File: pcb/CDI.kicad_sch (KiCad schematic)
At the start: 20 parts, among them Q1 MMBT2222A

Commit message: small fix
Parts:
- C9: footprint Capacitor_THT:CP_Axial_L18.0mm_D8.0mm_P25.00mm_Horizontal -> Capacitor_THT:C_Axial_L12.0mm_D7.5mm_P20.00mm_Horizontal
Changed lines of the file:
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@@
 			)
 		)
-		(property "Footprint" "Capacitor_THT:CP_Axial_L18.0mm_D8.0mm_P25.00mm_Horizontal"
+		(property "Footprint" "Capacitor_THT:C_Axial_L12.0mm_D7.5mm_P20.00mm_Horizontal"
 			(at 224.79 51.1048 0)
 			(effects

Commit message: video call revision
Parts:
- removed C10: 100n, Capacitor_SMD:C_0201_0603Metric, symbol Device:C
- removed JP6: SolderJumper_2_Open, Jumper:SolderJumper-2_P1.3mm_Open_RoundedPad1.0x1.5mm, symbol Jumper:SolderJumper_2_Open
- removed R14: 130R, Resistor_THT:R_Axial_DIN0204_L3.6mm_D1.6mm_P1.90mm_Vertical, symbol Device:R
- removed R16: 100R, Resistor_THT:R_Axial_DIN0204_L3.6mm_D1.6mm_P1.90mm_Vertical, symbol Device:R
- removed R17: 47k, Resistor_SMD:R_0201_0603Metric, symbol Device:R
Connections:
- net GND is gone; now on an unnamed net: Q1.2 (E)
- net +5V: now also Q1.3 (C)
- net at R13.1: no longer Q1.3 (C)
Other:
- note removed: "GATE SNUBBER"
- moved on the sheet: Q1, R15, TP9

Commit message: added footprints
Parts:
- D2: footprint TN1215800GTR -> SamacSys_Parts:TN1215800GTR
- TP10, TP11, TP9: footprint (none) -> Connector_PinHeader_1.00mm:PinHeader_1x01_P1.00mm_Vertical
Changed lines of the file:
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@@
 			)
 		)
-		(property "Footprint" ""
+		(property "Footprint" "Connector_PinHeader_1.00mm:PinHeader_1x01_P1.00mm_Vertical"
 			(at 123.19 59.69 0)
 			(effects
@@
 			)
 		)
-		(property "Footprint" ""
+		(property "Footprint" "Connector_PinHeader_1.00mm:PinHeader_1x01_P1.00mm_Vertical"
 			(at 175.26 44.45 0)
 			(effects
@@
 			)
 		)
-		(property "Footprint" ""
+		(property "Footprint" "Connector_PinHeader_1.00mm:PinHeader_1x01_P1.00mm_Vertical"
 			(at 240.03 44.45 0)
 			(effects
@@
 			)
 		)
-		(property "Footprint" "TN1215800GTR"
+		(property "Footprint" "SamacSys_Parts:TN1215800GTR"
 			(at 181.61 74.93 0)
 			(effects

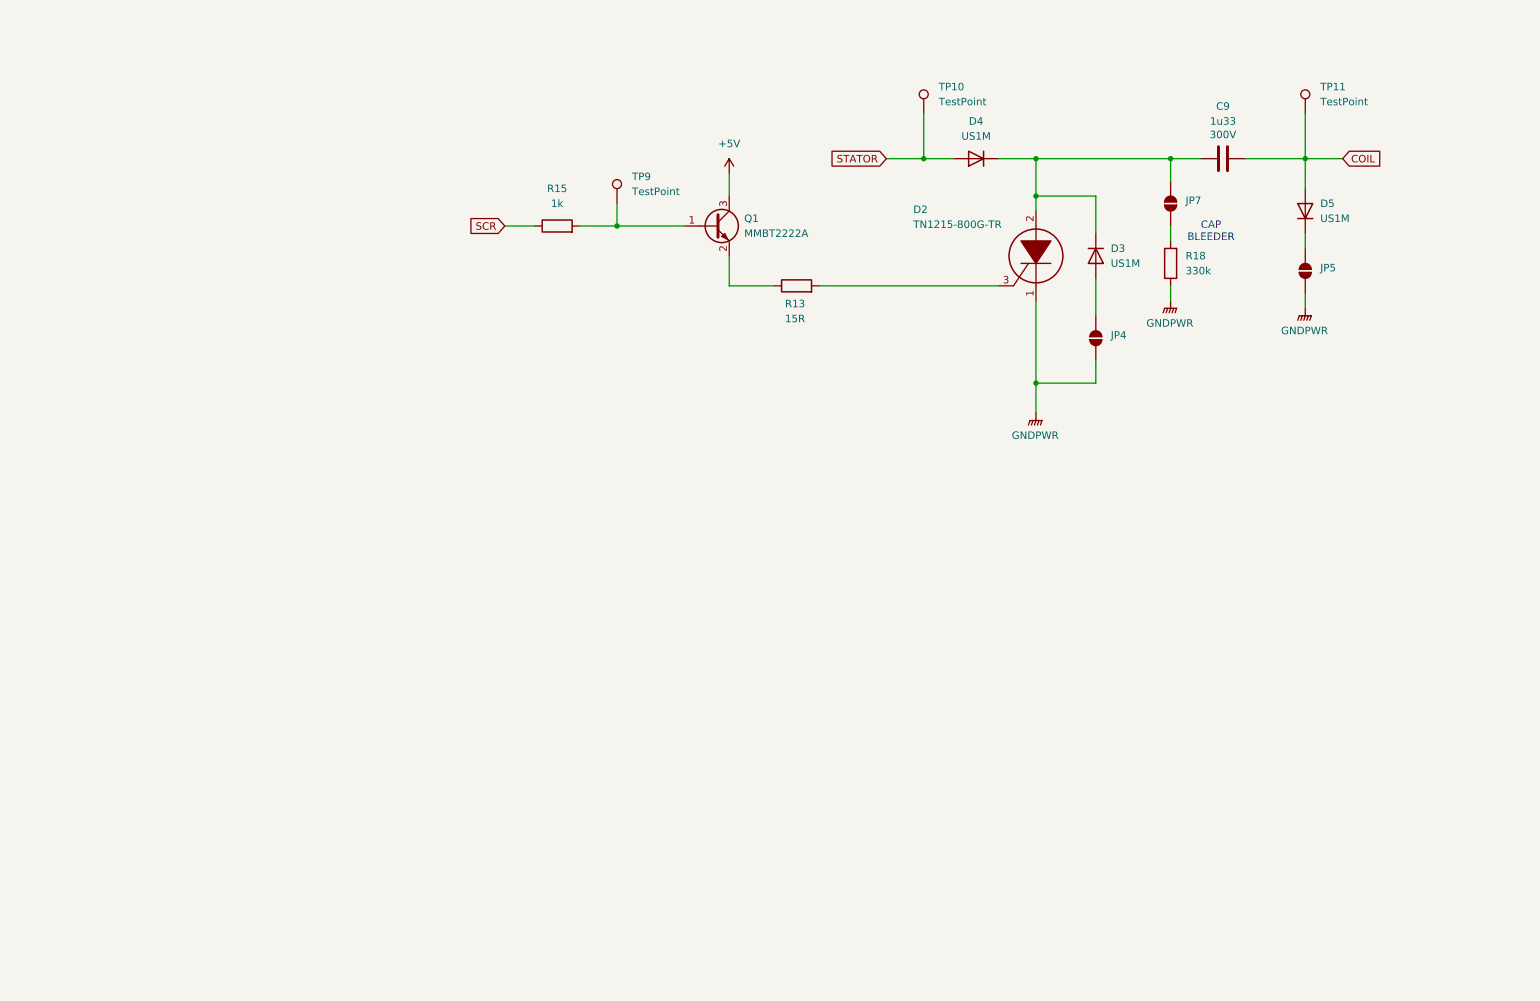
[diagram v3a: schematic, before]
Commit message: added SCR from kill switch to GND and RGB led
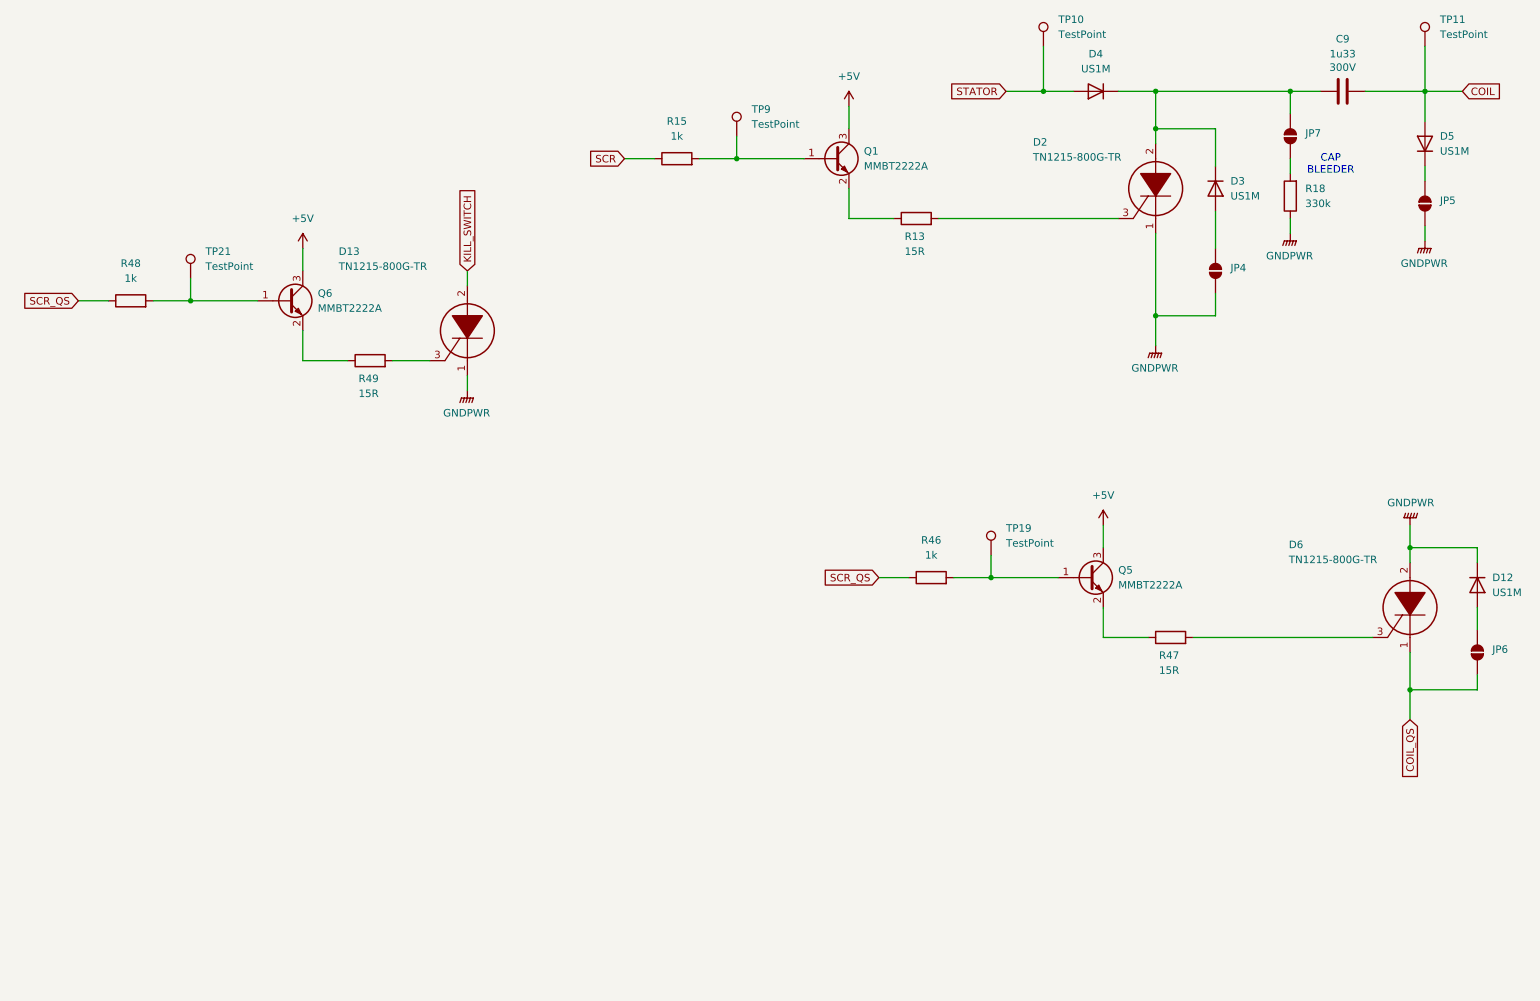
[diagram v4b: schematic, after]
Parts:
- added D12: US1M, Diode_SMD:D_SMA, symbol Diode:US1M
- added D13, D6: TN1215-800G-TR, SamacSys_Parts:TN1215800GTR, symbol SamacSys_Parts:TN1215-800G-TR
- added JP6: SolderJumper_2_Open, Jumper:SolderJumper-2_P1.3mm_Open_RoundedPad1.0x1.5mm, symbol Jumper:SolderJumper_2_Open
- added Q5, Q6: MMBT2222A, Package_TO_SOT_SMD:SOT-23, symbol Transistor_BJT:MMBT2222A
- added R46, R48: 1k, Resistor_SMD:R_0201_0603Metric, symbol Device:R
- added R47, R49: 15R, Resistor_THT:R_Axial_DIN0204_L3.6mm_D1.6mm_P1.90mm_Vertical, symbol Device:R
- added TP19, TP21: TestPoint, Connector_PinHeader_1.00mm:PinHeader_1x01_P1.00mm_Vertical, symbol Connector:TestPoint
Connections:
- net +5V: now also Q5.3 (C), Q6.3 (C)
- net GNDPWR: now also D12.1 (K), D13.1, D6.2
- new net: D13.3, R49.2
- new net: Q6.1 (B), R48.2, TP21.1
- new net: Q6.2 (E), R49.1
- new net: D6.3, R47.2
- new net: Q5.1 (B), R46.2, TP19.1
- new net: Q5.2 (E), R47.1
- new net: D12.2 (A), JP6.2 (B)
- new net COIL_QS: D6.1, JP6.1 (A)
- new net KILL_SWITCH: D13.2
- new net SCR_QS: R46.1, R48.1
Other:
- moved on the sheet: C9, D2, D3, D4, D5, JP4, JP5, JP7, Q1, R13, R15, R18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

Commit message: added connector and simulation link
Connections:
- net SCR_QS: no longer R48.1
- new net SCR_QS_KS: R48.1
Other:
- moved on the sheet: D13, Q6, R48, R49, TP21
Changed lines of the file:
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@@
 	)
 	(junction
-		(at 45.72 76.2)
+		(at 64.77 124.46)
 		(diameter 0)
 		(color 0 0 0 0)
@@
 	(wire
 		(pts
-			(xy 92.71 71.12) (xy 92.71 73.66)
+			(xy 111.76 119.38) (xy 111.76 121.92)
 		)
 		(stroke
@@
 	(wire
 		(pts
-			(xy 72.39 86.36) (xy 64.77 86.36)
+			(xy 91.44 134.62) (xy 83.82 134.62)
 		)
 		(stroke
@@
 	(wire
 		(pts
-			(xy 26.67 76.2) (xy 31.75 76.2)
+			(xy 45.72 124.46) (xy 50.8 124.46)
 		)
 		(stroke
@@
 	(wire
 		(pts
-			(xy 92.71 91.44) (xy 92.71 88.9)
+			(xy 111.76 139.7) (xy 111.76 137.16)
 		)
 		(stroke
@@
 	(wire
 		(pts
-			(xy 80.01 86.36) (xy 86.36 86.36)
+			(xy 99.06 134.62) (xy 105.41 134.62)
 		)
 		(stroke
@@
 	(wire
 		(pts
-			(xy 64.77 67.31) (xy 64.77 71.12)
+			(xy 83.82 115.57) (xy 83.82 119.38)
 		)
 		(stroke
@@
 	(wire
 		(pts
-			(xy 45.72 72.39) (xy 45.72 76.2)
+			(xy 64.77 120.65) (xy 64.77 124.46)
 		)
 		(stroke
@@
 	(wire
 		(pts
-			(xy 45.72 76.2) (xy 57.15 76.2)
+			(xy 64.77 124.46) (xy 76.2 124.46)
 		)
 		(stroke
@@
 	(wire
 		(pts
-			(xy 64.77 81.28) (xy 64.77 86.36)
+			(xy 83.82 129.54) (xy 83.82 134.62)
 		)
 		(stroke
@@
 	(wire
 		(pts
-			(xy 39.37 76.2) (xy 45.72 76.2)
+			(xy 58.42 124.46) (xy 64.77 124.46)
 		)
 		(stroke
@@
 		)
 	)
-	(global_label "SCR_QS"
+	(global_label "SCR_QS_KS"
 		(shape input)
-		(at 26.67 76.2 180)
+		(at 45.72 124.46 180)
 		(fields_autoplaced yes)
 		(effects
@@
 		)
 		(property "Intersheetrefs" "${INTERSHEET_REFS}"
-			(at 16.4277 76.2 0)
+			(at 32.0306 124.46 0)
 			(effects
 				(font
@@
 	(global_label "KILL_SWITCH"
 		(shape input)
-		(at 92.71 71.12 90)
+		(at 111.76 119.38 90)
 		(fields_autoplaced yes)
 		(effects
@@
 		)
 		(property "Intersheetrefs" "${INTERSHEET_REFS}"
-			(at 92.71 56.4024 90)
+			(at 111.76 104.6624 90)
 			(effects
 				(font
@@
 	(symbol
 		(lib_id "SamacSys_Parts:TN1215-800G-TR")
-		(at 92.71 73.66 270)
+		(at 111.76 121.92 270)
 		(unit 1)
 		(exclude_from_sim no)
@@
 		(dnp no)
 		(property "Reference" "D13"
-			(at 70.866 67.818 90)
+			(at 89.916 116.078 90)
 			(effects
 				(font
@@
 		)
 		(property "Value" "TN1215-800G-TR"
-			(at 70.866 70.358 90)
+			(at 89.916 118.618 90)
 			(effects
 				(font
@@
 		)
 		(property "Footprint" "SamacSys_Parts:TN1215800GTR"
-			(at 85.09 87.63 0)
+			(at 104.14 135.89 0)
 			(effects
 				(font
@@
 		)
 		(property "Datasheet" "https://www.st.com/resource/en/datasheet/tyn1012.pdf"
-			(at 82.55 87.63 0)
+			(at 101.6 135.89 0)
 			(effects
 				(font
@@
 		)
 		(property "Description" "12A standard SCRs"
-			(at 92.71 73.66 0)
+			(at 111.76 121.92 0)
 			(effects
 				(font
@@
 		)
 		(property "Description_1" "12A standard SCRs"
-			(at 80.01 87.63 0)
+			(at 99.06 135.89 0)
 			(effects
 				(font
@@
 		)
 		(property "Height" "4.83"
-			(at 77.47 87.63 0)
+			(at 96.52 135.89 0)
 			(effects
 				(font
@@
 		)
 		(property "Manufacturer_Name" "STMicroelectronics"
-			(at 74.93 87.63 0)
+			(at 93.98 135.89 0)
 			(effects
 				(font
@@
 		)
 		(property "Manufacturer_Part_Number" "TN1215-800G-TR"
-			(at 72.39 87.63 0)
+			(at 91.44 135.89 0)
 			(effects
 				(font
@@
 		)
 		(property "Mouser Part Number" "511-TN1215-800G-TR"
-			(at 69.85 87.63 0)
+			(at 88.9 135.89 0)
 			(effects
 				(font
@@
 		)
 		(property "Mouser Price/Stock" "https://www.mouser.co.uk/ProductDetail/STMicroelectronics/TN1215-800G-TR?qs=wzLlR2ZSnfOWcDyT875ztQ%3D%3D"
-			(at 67.31 87.63 0)
+			(at 86.36 135.89 0)
 			(effects
 				(font
@@
 		)
 		(property "Arrow Part Number" "TN1215-800G-TR"
-			(at 64.77 87.63 0)
+			(at 83.82 135.89 0)
 			(effects
 				(font
@@
 		)
 		(property "Arrow Price/Stock" "https://www.arrow.com/en/products/tn1215-800g-tr/stmicroelectronics?utm_currency=USD&region=nac"
-			(at 62.23 87.63 0)
+			(at 81.28 135.89 0)
 			(effects
 				(font
@@
 	(symbol
 		(lib_id "Transistor_BJT:MMBT2222A")
-		(at 62.23 76.2 0)
+		(at 81.28 124.46 0)
 		(unit 1)
 		(exclude_from_sim no)
@@
 		(fields_autoplaced yes)
 		(property "Reference" "Q6"
-			(at 67.31 74.9299 0)
+			(at 86.36 123.1899 0)
 			(effects
 				(font
@@
 		)
 		(property "Value" "MMBT2222A"
-			(at 67.31 77.4699 0)
+			(at 86.36 125.7299 0)
 			(effects
 				(font
@@
 		)
 		(property "Footprint" "Package_TO_SOT_SMD:SOT-23"
-			(at 67.31 78.105 0)
+			(at 86.36 126.365 0)
 			(effects
 				(font
@@
 		)
 		(property "Datasheet" "https://assets.nexperia.com/documents/data-sheet/MMBT2222A.pdf"
-			(at 62.23 76.2 0)
+			(at 81.28 124.46 0)
 			(effects
 				(font
@@
 		)
 		(property "Description" "600mA Ic, 40V Vce, NPN Transistor, SOT-23"
-			(at 62.23 76.2 0)
+			(at 81.28 124.46 0)
 			(effects
 				(font
@@
 	(symbol
 		(lib_id "Device:R")
-		(at 76.2 86.36 90)
+		(at 95.25 134.62 90)
 		(unit 1)
 		(exclude_from_sim no)
@@
 		(dnp no)
 		(property "Reference" "R49"
-			(at 75.946 89.408 90)
+			(at 94.996 137.668 90)
 			(effects
 				(font
@@
 		)
 		(property "Value" "15R"
-			(at 75.946 91.948 90)
+			(at 94.996 140.208 90)
 			(effects
 				(font
@@
 		)
 		(property "Footprint" "Resistor_THT:R_Axial_DIN0204_L3.6mm_D1.6mm_P1.90mm_Vertical"
-			(at 76.2 88.138 90)
+			(at 95.25 136.398 90)
 			(effects
 				(font
@@
 		)
 		(property "Datasheet" "~"
-			(at 76.2 86.36 0)
+			(at 95.25 134.62 0)
 			(effects
 				(font
@@
 		)
 		(property "Description" "Resistor"
-			(at 76.2 86.36 0)
+			(at 95.25 134.62 0)
 			(effects
 				(font
@@
 	(symbol
 		(lib_id "power:GNDPWR")
-		(at 92.71 91.44 0)
+		(at 111.76 139.7 0)
 		(unit 1)
 		(exclude_from_sim no)
@@
 		(fields_autoplaced yes)
 		(property "Reference" "#PWR052"
-			(at 92.71 96.52 0)
+			(at 111.76 144.78 0)
 			(effects
 				(font
@@
 		)
 		(property "Value" "GNDPWR"
-			(at 92.583 95.25 0)
+			(at 111.633 143.51 0)
 			(effects
 				(font
@@
 		)
 		(property "Footprint" ""
-			(at 92.71 92.71 0)
+			(at 111.76 140.97 0)
 			(effects
 				(font
@@
 		)
 		(property "Datasheet" ""
-			(at 92.71 92.71 0)
+			(at 111.76 140.97 0)
 			(effects
 				(font
@@
 		)
 		(property "Description" "Power symbol creates a global label with name \"GNDPWR\" , global ground"
-			(at 92.71 91.44 0)
+			(at 111.76 139.7 0)
 			(effects
 				(font
@@
 	(symbol
 		(lib_id "power:+5V")
-		(at 64.77 67.31 0)
+		(at 83.82 115.57 0)
 		(unit 1)
 		(exclude_from_sim no)
@@
 		(fields_autoplaced yes)
 		(property "Reference" "#PWR051"
-			(at 64.77 71.12 0)
+			(at 83.82 119.38 0)
 			(effects
 				(font
@@
 		)
 		(property "Value" "+5V"
-			(at 64.77 62.23 0)
+			(at 83.82 110.49 0)
 			(effects
 				(font
@@
 		)
 		(property "Footprint" ""
-			(at 64.77 67.31 0)
+			(at 83.82 115.57 0)
 			(effects
 				(font
@@
 		)
 		(property "Datasheet" ""
-			(at 64.77 67.31 0)
+			(at 83.82 115.57 0)
 			(effects
 				(font
@@
 		)
 		(property "Description" "Power symbol creates a global label with name \"+5V\""
-			(at 64.77 67.31 0)
+			(at 83.82 115.57 0)
 			(effects
 				(font
@@
 	(symbol
 		(lib_id "Connector:TestPoint")
-		(at 45.72 72.39 0)
+		(at 64.77 120.65 0)
 		(unit 1)
 		(exclude_from_sim no)
@@
 		(fields_autoplaced yes)
 		(property "Reference" "TP21"
-			(at 48.26 67.8179 0)
+			(at 67.31 116.0779 0)
 			(effects
 				(font
@@
 		)
 		(property "Value" "TestPoint"
-			(at 48.26 70.3579 0)
+			(at 67.31 118.6179 0)
 			(effects
 				(font
@@
 		)
 		(property "Footprint" "Connector_PinHeader_1.00mm:PinHeader_1x01_P1.00mm_Vertical"
-			(at 50.8 72.39 0)
+			(at 69.85 120.65 0)
 			(effects
 				(font
@@
 		)
 		(property "Datasheet" "~"
-			(at 50.8 72.39 0)
+			(at 69.85 120.65 0)
 			(effects
 				(font
@@
 		)
 		(property "Description" "test point"
-			(at 45.72 72.39 0)
+			(at 64.77 120.65 0)
 			(effects
 				(font
@@
 	(symbol
 		(lib_id "Device:R")
-		(at 35.56 76.2 90)
+		(at 54.61 124.46 90)
 		(unit 1)
 		(exclude_from_sim no)
@@
 		(fields_autoplaced yes)
 		(property "Reference" "R48"
-			(at 35.56 69.85 90)
+			(at 54.61 118.11 90)
 			(effects
 				(font
@@
 		)
 		(property "Value" "1k"
-			(at 35.56 72.39 90)
+			(at 54.61 120.65 90)
 			(effects
 				(font
@@
 		)
 		(property "Footprint" "Resistor_SMD:R_0201_0603Metric"
-			(at 35.56 77.978 90)
+			(at 54.61 126.238 90)
 			(effects
 				(font
@@
 		)
 		(property "Datasheet" "~"
-			(at 35.56 76.2 0)
+			(at 54.61 124.46 0)
 			(effects
 				(font
@@
 		)
 		(property "Description" "Resistor"
-			(at 35.56 76.2 0)
+			(at 54.61 124.46 0)
 			(effects
 				(font

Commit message: changed capacitors and resistors footprints from 0201 to 0603
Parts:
- R15, R18, R46, R48: footprint Resistor_SMD:R_0201_0603Metric -> Resistor_SMD:R_0603_1608Metric
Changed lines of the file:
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@@
 			)
 		)
-		(property "Footprint" "Resistor_SMD:R_0201_0603Metric"
+		(property "Footprint" "Resistor_SMD:R_0603_1608Metric"
 			(at 128.27 53.848 90)
 			(effects
@@
 			)
 		)
-		(property "Footprint" "Resistor_SMD:R_0201_0603Metric"
+		(property "Footprint" "Resistor_SMD:R_0603_1608Metric"
 			(at 234.188 58.42 90)
 			(effects
@@
 			)
 		)
-		(property "Footprint" "Resistor_SMD:R_0201_0603Metric"
+		(property "Footprint" "Resistor_SMD:R_0603_1608Metric"
 			(at 171.45 124.968 90)
 			(effects
@@
 			)
 		)
-		(property "Footprint" "Resistor_SMD:R_0201_0603Metric"
+		(property "Footprint" "Resistor_SMD:R_0603_1608Metric"
 			(at 54.61 126.238 90)
 			(effects
